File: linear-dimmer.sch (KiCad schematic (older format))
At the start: 30 parts, among them CON1 BARREL_JACK, P1 POWER, Q1 BUK6207-55C, SW1 Switch_SPDT_x2, U1 LM78L05ACZ, U2 MCP6072, U3 REF3012, U4 MCP65R41T

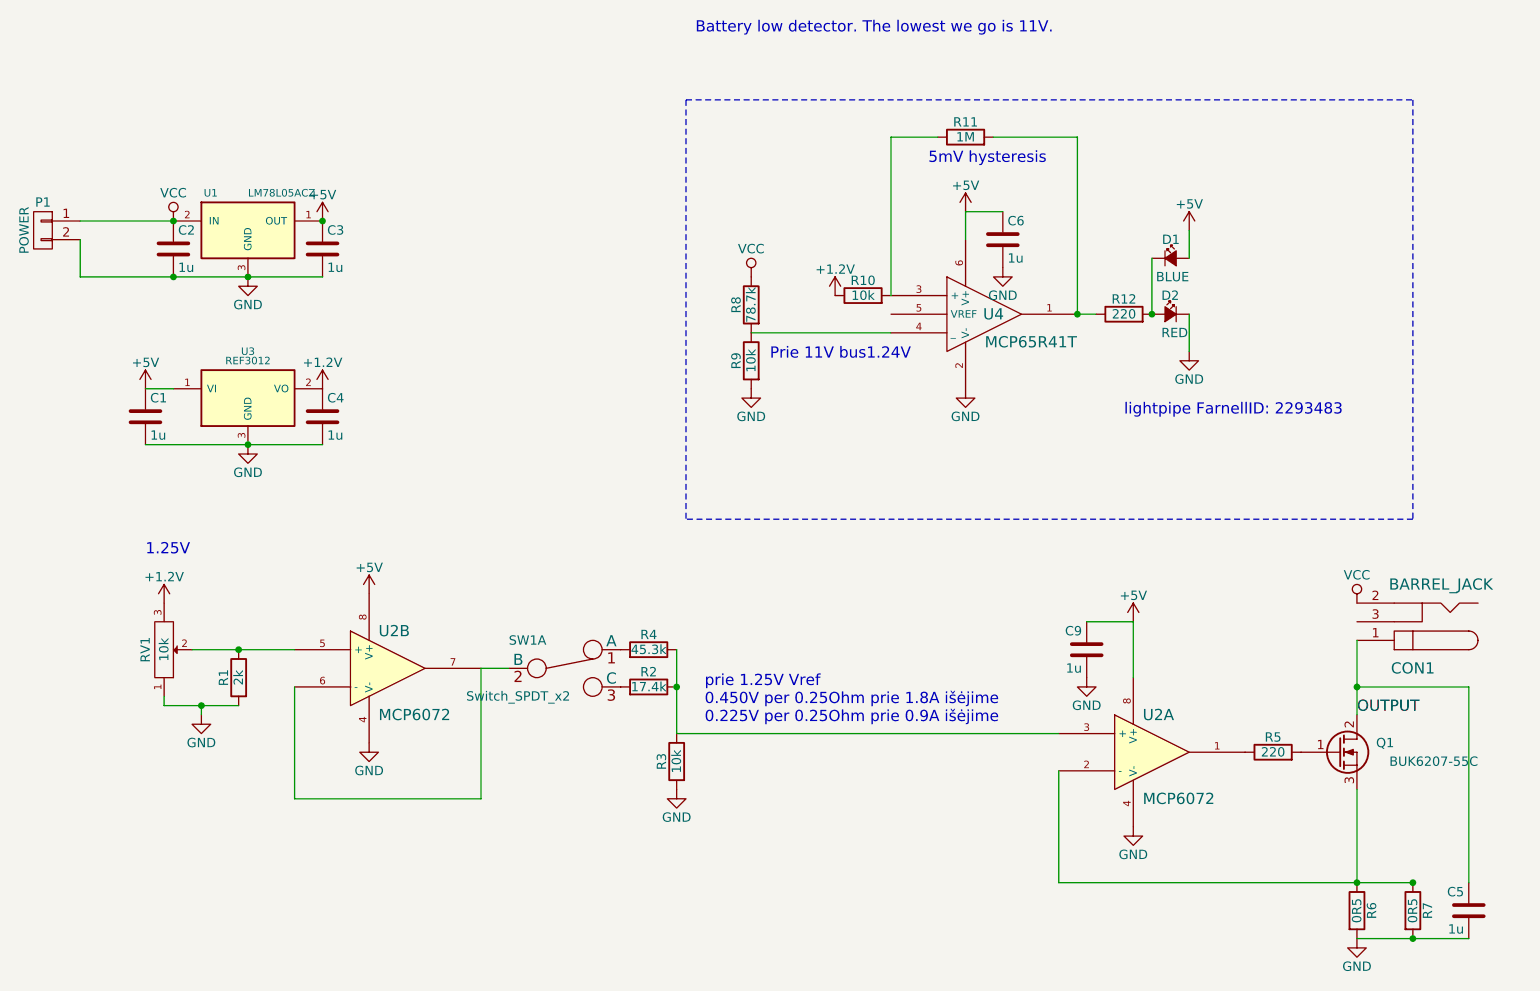
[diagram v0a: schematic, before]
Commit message: Add a dummy load resistor so that opamp will be forced to swing the output down at the lowest current setting turning the LEDs off
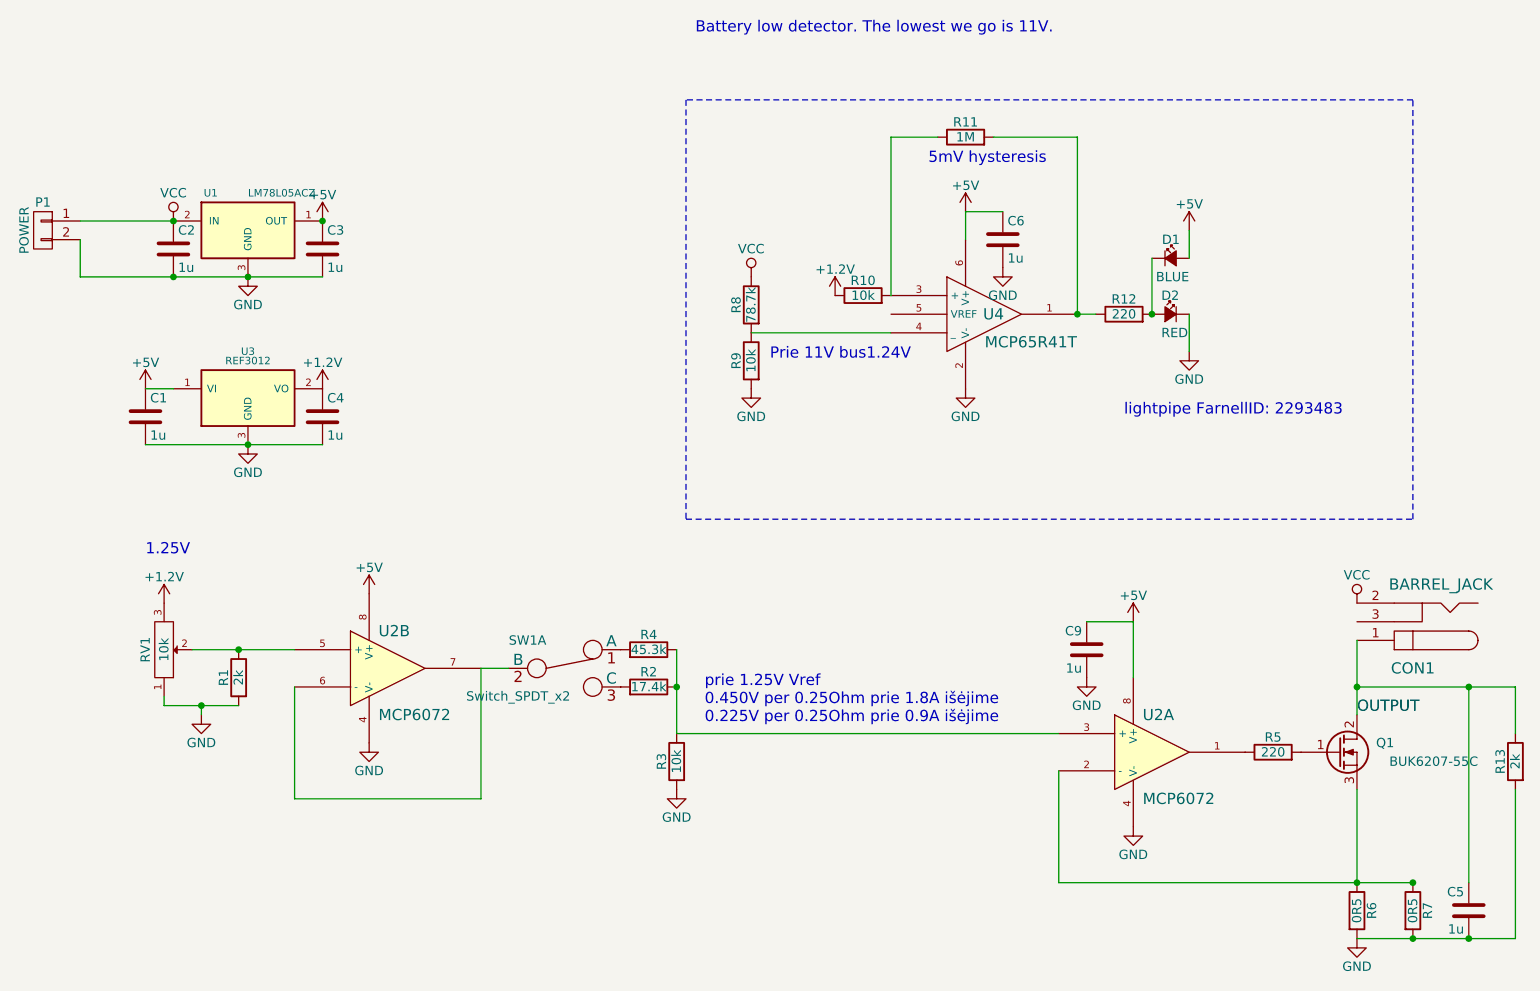
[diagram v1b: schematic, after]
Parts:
- added R13: 2k, Resistors_SMD:R_0603_HandSoldering, symbol R
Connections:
- net GND: now also R13.2
- net OUTPUT: now also R13.1
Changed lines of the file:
@@
 Connection ~ 8900 5450
 Wire Wire Line
-	8900 5750 9500 5750
+	8900 5750 9750 5750
 Wire Wire Line
 	7450 4050 7700 4050
@@
 	5300 1250 5300 3500
 Wire Notes Line
-	9200 3500 5300 3500
+	5300 3500 9200 3500
 Wire Notes Line
-	9200 1250 9200 3500
+	9200 3500 9200 1250
 Text Notes 5350 900  0    60   ~ 0
 Battery low detector. The lowest we go is 11V.
@@
 	9500 5450 9500 4400
 Wire Wire Line
-	9500 4400 8900 4400
+	8900 4400 9750 4400
 Connection ~ 8900 4400
 Connection ~ 7800 2400
@@
 	7400 1450 7400 2400
 Wire Notes Line
-	5300 1250 9200 1250
+	9200 1250 5300 1250
+$Comp
+L R R13
+U 1 1 562B7842
+P 9750 4800
+F 0 "R13" V 9830 4800 50  0000 C CNN
+F 1 "2k" V 9750 4800 50  0000 C CNN
+F 2 "Resistors_SMD:R_0603_HandSoldering" V 9680 4800 30  0001 C CNN
+F 3 "" H 9750 4800 30  0000 C CNN
+	1    9750 4800
+	-1   0    0    -1
+$EndComp
+Wire Wire Line
+	9750 4400 9750 4650
+Connection ~ 9500 4400
+Wire Wire Line
+	9750 5750 9750 4950
+Connection ~ 9500 5750
 $EndSCHEMATC

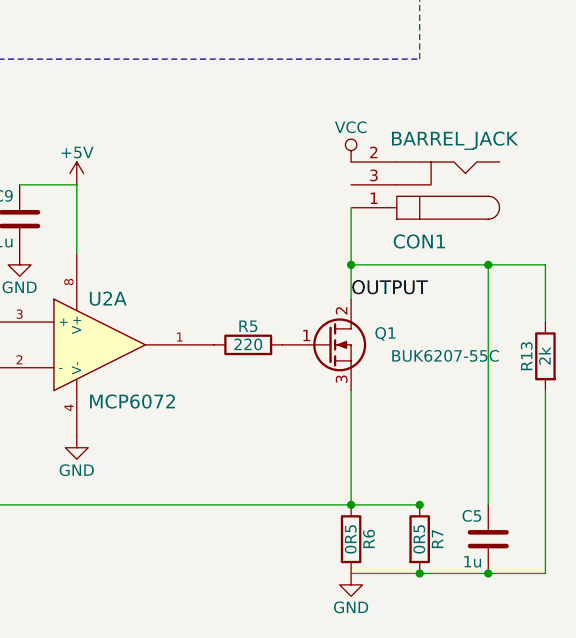
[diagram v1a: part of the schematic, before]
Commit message: Put load to the proper place in schematics
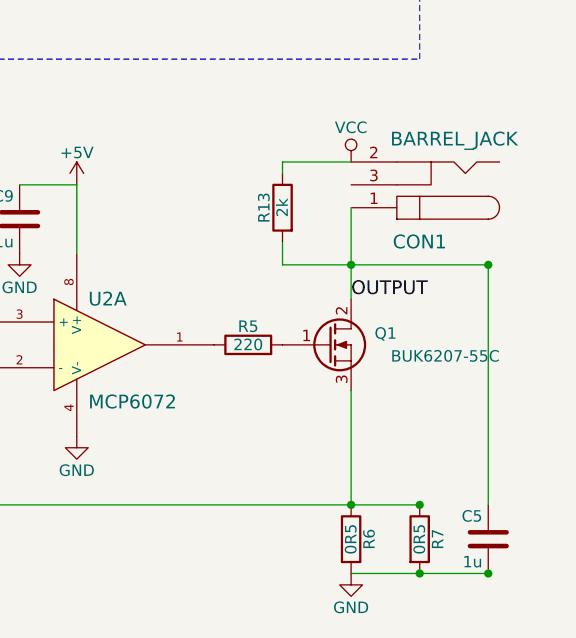
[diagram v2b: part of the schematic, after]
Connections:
- net GND: no longer R13.2
- net OUTPUT: now also R13.2; no longer R13.1
- net VCC: now also R13.1
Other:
- moved on the sheet: R13
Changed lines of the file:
@@
 Connection ~ 8900 5450
-Wire Wire Line
-	8900 5750 9750 5750
 Wire Wire Line
 	7450 4050 7700 4050
@@
 	7300 5450 9200 5450
 Wire Wire Line
-	9500 5450 9500 4400
-Wire Wire Line
-	8900 4400 9750 4400
+	9500 4400 9500 5450
 Connection ~ 8900 4400
 Connection ~ 7800 2400
@@
 L R R13
 U 1 1 562B7842
-P 9750 4800
-F 0 "R13" V 9830 4800 50  0000 C CNN
-F 1 "2k" V 9750 4800 50  0000 C CNN
-F 2 "Resistors_SMD:R_0603_HandSoldering" V 9680 4800 30  0001 C CNN
-F 3 "" H 9750 4800 30  0000 C CNN
-	1    9750 4800
+P 8600 4150
+F 0 "R13" V 8680 4150 50  0000 C CNN
+F 1 "2k" V 8600 4150 50  0000 C CNN
+F 2 "Resistors_SMD:R_0603_HandSoldering" V 8530 4150 30  0001 C CNN
+F 3 "" H 8600 4150 30  0000 C CNN
+	1    8600 4150
 	-1   0    0    -1
 $EndComp
-Wire Wire Line
-	9750 4400 9750 4650
 Connection ~ 9500 4400
-Wire Wire Line
-	9750 5750 9750 4950
 Connection ~ 9500 5750
+Wire Wire Line
+	8900 5750 9500 5750
+Wire Wire Line
+	8600 4400 9500 4400
+Wire Wire Line
+	8600 4300 8600 4400
+Wire Wire Line
+	8600 4000 8600 3950
+Wire Wire Line
+	8600 3950 8900 3950
 $EndSCHEMATC

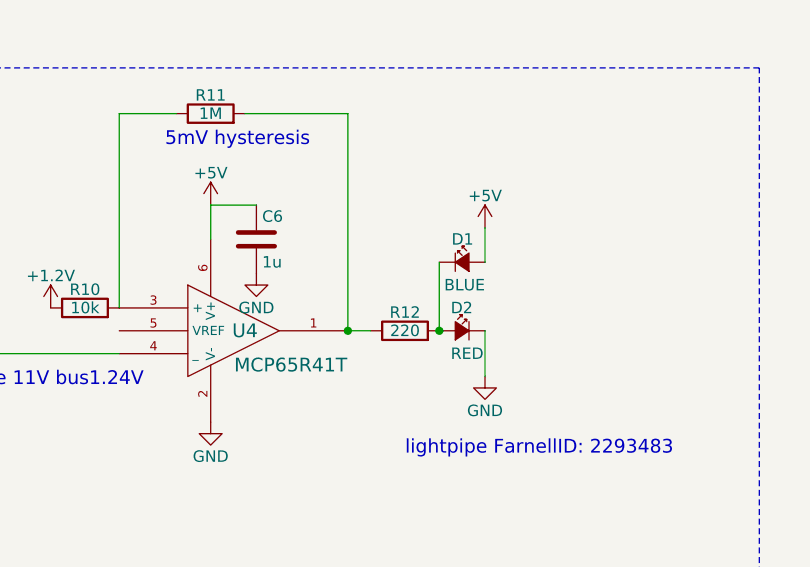
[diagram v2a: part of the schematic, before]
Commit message: Add a resistor for the blue led to embarass less
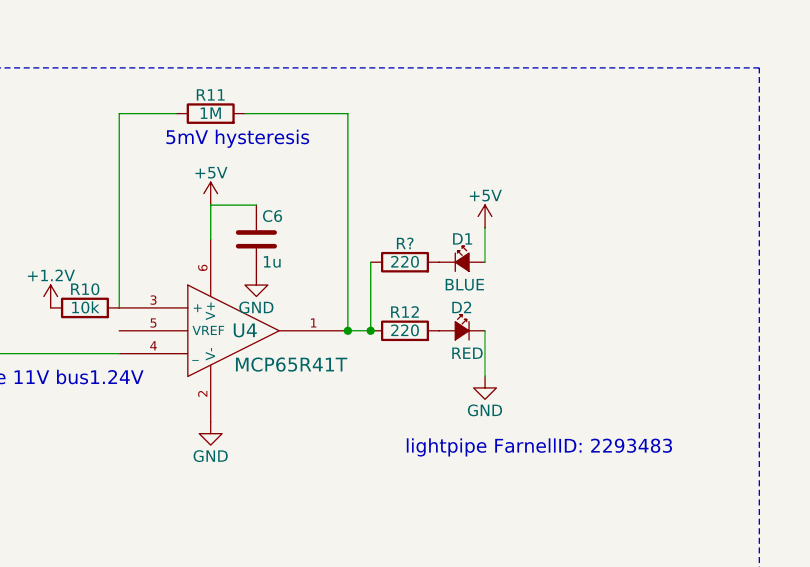
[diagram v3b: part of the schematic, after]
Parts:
- added R?: 220, Resistors_SMD:R_0603_HandSoldering, symbol R
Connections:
- net at D2.1 (A), R12.2: no longer D1.2 (C)
- net at R11.2, R12.1, U4.1: now also R?.1
- new net: D1.2 (C), R?.2
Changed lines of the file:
@@
 	9500 4400 9500 5450
 Connection ~ 8900 4400
-Connection ~ 7800 2400
 $Comp
 L +5V #PWR024
@@
 $EndComp
 Wire Wire Line
-	7800 2400 7800 2100
+	7800 2100 7800 2100
 Wire Wire Line
 	8000 1950 8000 2100
@@
 Wire Wire Line
 	8600 3950 8900 3950
+$Comp
+L R R?
+U 1 1 566F30FA
+P 7650 2100
+F 0 "R?" V 7730 2100 50  0000 C CNN
+F 1 "220" V 7650 2100 50  0000 C CNN
+F 2 "Resistors_SMD:R_0603_HandSoldering" V 7580 2100 30  0001 C CNN
+F 3 "" H 7650 2100 30  0000 C CNN
+	1    7650 2100
+	0    -1   -1   0
+$EndComp
+Wire Wire Line
+	7500 2400 7500 2100
+Connection ~ 7500 2400
 $EndSCHEMATC
